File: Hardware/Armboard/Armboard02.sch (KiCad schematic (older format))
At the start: 11 parts

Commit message: Imported footprints to layout
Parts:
- Gripper_Motor1: footprint (none) -> MRDT_ICs:MultiPowerSO_30
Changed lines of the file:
@@
 F 0 "Gripper_Motor1" H 5300 5237 60  0000 C CNN
 F 1 "VNH5019A_E" H 5300 5131 60  0000 C CNN
-F 2 "" H 4700 4850 60  0001 C CNN
+F 2 "MRDT_ICs:MultiPowerSO_30" H 4700 4850 60  0001 C CNN
 F 3 "" H 4700 4850 60  0001 C CNN
 	1    4700 3550

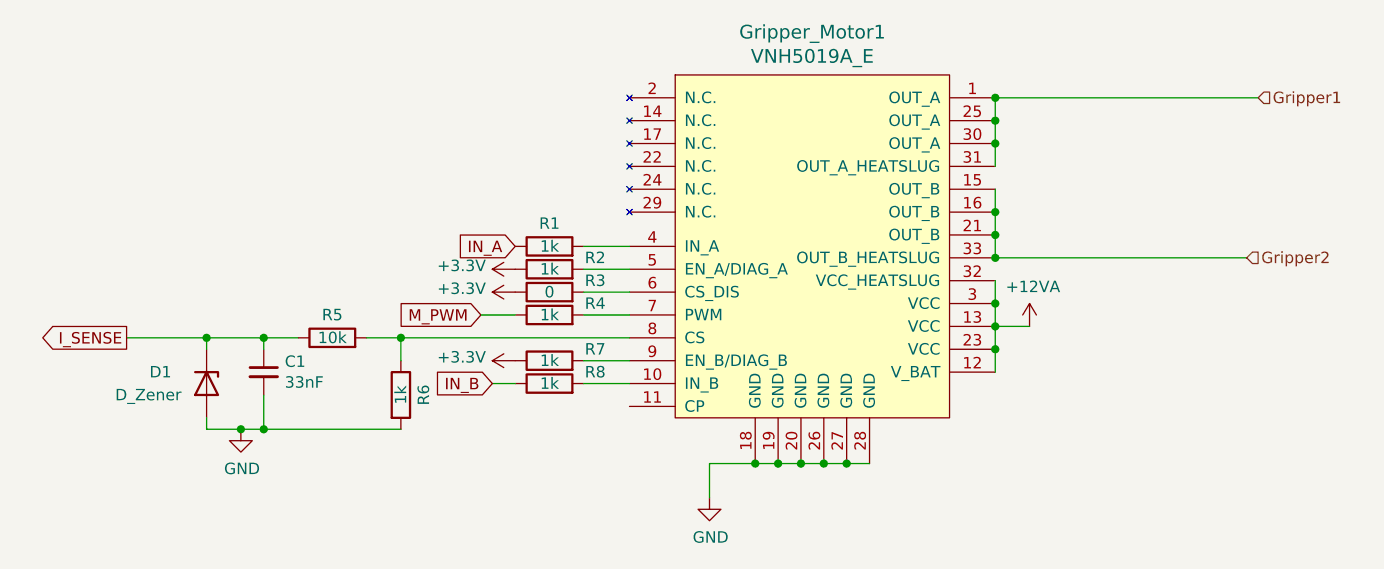
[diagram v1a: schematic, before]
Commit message: Double-checked schematic, pointed power pins up, made sure 12V and 3.3V were full networks
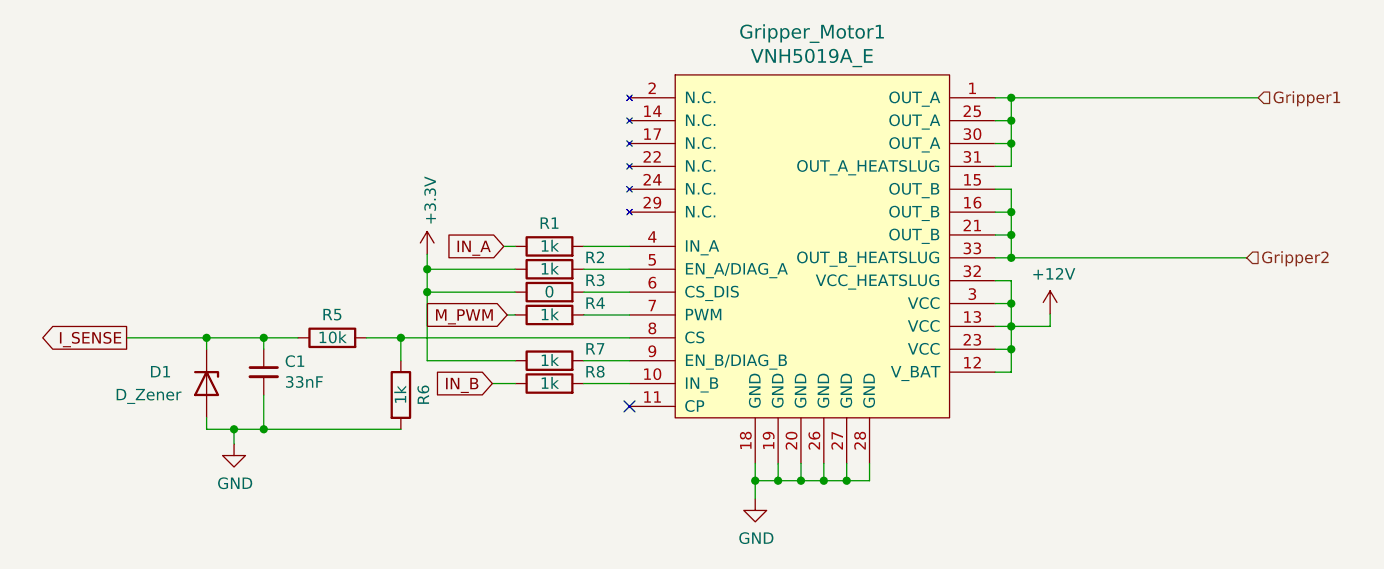
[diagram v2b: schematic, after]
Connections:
- net +12VA renamed +12V
- no-connect marks 0 -> 1
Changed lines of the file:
@@
 $EndDescr
-$Comp
-L MRDT_ICs:VNH5019A_E Gripper_Motor1
-U 1 1 5F7F9831
-P 4700 3550
-F 0 "Gripper_Motor1" H 5300 5237 60  0000 C CNN
-F 1 "VNH5019A_E" H 5300 5131 60  0000 C CNN
-F 2 "MRDT_ICs:MultiPowerSO_30" H 4700 4850 60  0001 C CNN
-F 3 "" H 4700 4850 60  0001 C CNN
-	1    4700 3550
-	1    0    0    -1
-$EndComp
 $Comp
 L power:GND #PWR074
 U 1 1 5F7FB309
-P 4850 3900
-F 0 "#PWR074" H 4850 3650 50  0001 C CNN
-F 1 "GND" H 4855 3727 50  0000 C CNN
-F 2 "" H 4850 3900 50  0001 C CNN
-F 3 "" H 4850 3900 50  0001 C CNN
-	1    4850 3900
-	1    0    0    -1
-$EndComp
-Wire Wire Line
-	5550 3750 5450 3750
-Connection ~ 5150 3750
-Wire Wire Line
-	5150 3750 5050 3750
-Connection ~ 5250 3750
-Wire Wire Line
-	5250 3750 5150 3750
-Connection ~ 5350 3750
-Wire Wire Line
-	5350 3750 5250 3750
-Connection ~ 5450 3750
-Wire Wire Line
-	5450 3750 5350 3750
-Wire Wire Line
-	5050 3750 4850 3750
-Wire Wire Line
-	4850 3750 4850 3900
-Connection ~ 5050 3750
-Wire Wire Line
-	6100 2150 6100 2250
-Connection ~ 6100 2250
-Wire Wire Line
-	6100 2250 6100 2350
-Connection ~ 6100 2350
-Wire Wire Line
-	6100 2350 6100 2450
-Connection ~ 6100 2150
-Wire Wire Line
-	6100 2550 6100 2650
-Connection ~ 6100 2650
-Wire Wire Line
-	6100 2650 6100 2750
-Connection ~ 6100 2750
-Wire Wire Line
-	6100 2750 6100 2850
-Wire Wire Line
-	6100 2950 6100 3050
-Connection ~ 6100 3050
-Wire Wire Line
-	6100 3050 6100 3150
-Connection ~ 6100 3150
-Wire Wire Line
-	6100 3150 6100 3250
-Connection ~ 6100 3250
-Wire Wire Line
-	6100 3250 6100 3350
-Wire Wire Line
-	6100 3150 6250 3150
-$Comp
-L power:+12VA #PWR075
-U 1 1 5F7FD222
-P 6250 3150
-F 0 "#PWR075" H 6250 3000 50  0001 C CNN
-F 1 "+12VA" H 6265 3323 50  0000 C CNN
-F 2 "" H 6250 3150 50  0001 C CNN
-F 3 "" H 6250 3150 50  0001 C CNN
-	1    6250 3150
+P 5050 3905
+F 0 "#PWR074" H 5050 3655 50  0001 C CNN
+F 1 "GND" H 5055 3732 50  0000 C CNN
+F 2 "" H 5050 3905 50  0001 C CNN
+F 3 "" H 5050 3905 50  0001 C CNN
+	1    5050 3905
 	1    0    0    -1
 $EndComp
@@
 L power:+3.3V #PWR071
 U 1 1 5F802765
-P 4000 2900
-F 0 "#PWR071" H 4000 2750 50  0001 C CNN
-F 1 "+3.3V" V 4015 3028 50  0000 L CNN
-F 2 "" H 4000 2900 50  0001 C CNN
-F 3 "" H 4000 2900 50  0001 C CNN
-	1    4000 2900
-	0    -1   -1   0
+P 3615 2835
+F 0 "#PWR071" H 3615 2685 50  0001 C CNN
+F 1 "+3.3V" V 3630 2963 50  0000 L CNN
+F 2 "" H 3615 2835 50  0001 C CNN
+F 3 "" H 3615 2835 50  0001 C CNN
+	1    3615 2835
+	1    0    0    -1
 $EndComp
 $Comp
@@
 	0    -1   -1   0
 $EndComp
-$Comp
-L power:+3.3V #PWR072
-U 1 1 5F807CCC
-P 4000 3000
-F 0 "#PWR072" H 4000 2850 50  0001 C CNN
-F 1 "+3.3V" V 4015 3128 50  0000 L CNN
-F 2 "" H 4000 3000 50  0001 C CNN
-F 3 "" H 4000 3000 50  0001 C CNN
-	1    4000 3000
-	0    -1   -1   0
-$EndComp
 Wire Wire Line
 	4300 3100 4500 3100
@@
 L power:GND #PWR070
 U 1 1 5F80DDCF
-P 2800 3600
-F 0 "#PWR070" H 2800 3350 50  0001 C CNN
-F 1 "GND" H 2805 3427 50  0000 C CNN
-F 2 "" H 2800 3600 50  0001 C CNN
-F 3 "" H 2800 3600 50  0001 C CNN
-	1    2800 3600
-	1    0    0    -1
-$EndComp
-Wire Wire Line
-	2900 3600 2800 3600
+P 2770 3665
+F 0 "#PWR070" H 2770 3415 50  0001 C CNN
+F 1 "GND" H 2775 3492 50  0000 C CNN
+F 2 "" H 2770 3665 50  0001 C CNN
+F 3 "" H 2770 3665 50  0001 C CNN
+	1    2770 3665
+	1    0    0    -1
+$EndComp
 Connection ~ 2900 3600
 Wire Wire Line
-	2800 3600 2650 3600
-Wire Wire Line
 	2650 3600 2650 3550
-Connection ~ 2800 3600
 Text GLabel 2300 3200 0    50   Output ~ 0
 I_SENSE
@@
 	0    -1   -1   0
 $EndComp
-$Comp
-L power:+3.3V #PWR073
-U 1 1 5F818EFA
-P 4000 3300
-F 0 "#PWR073" H 4000 3150 50  0001 C CNN
-F 1 "+3.3V" V 4015 3428 50  0000 L CNN
-F 2 "" H 4000 3300 50  0001 C CNN
-F 3 "" H 4000 3300 50  0001 C CNN
-	1    4000 3300
-	0    -1   -1   0
-$EndComp
 Wire Wire Line
 	3500 3200 4500 3200
 Wire Wire Line
-	6100 2150 7250 2150
-Connection ~ 6100 2850
-Wire Wire Line
-	6100 2850 7200 2850
-Wire Wire Line
-	3850 3100 4000 3100
+	6100 2150 6170 2150
+Wire Wire Line
+	6100 2850 6170 2850
 Wire Wire Line
 	4000 3400 3900 3400
 Text GLabel 3900 3400 0    50   Input ~ 0
 IN_B
-Text GLabel 4000 2800 0    50   Input ~ 0
+Text GLabel 3950 2800 0    50   Input ~ 0
 IN_A
-Text GLabel 3850 3100 0    50   Input ~ 0
+Text GLabel 3965 3100 0    50   Input ~ 0
 M_PWM
 Text HLabel 7250 2150 2    50   Input ~ 0
@@
 	0    1    1    0
 $EndComp
+Wire Wire Line
+	4000 3000 3615 3000
+Wire Wire Line
+	3615 3000 3615 2900
+Wire Wire Line
+	4000 2900 3615 2900
+Connection ~ 3615 2900
+Wire Wire Line
+	3615 2900 3615 2835
+Wire Wire Line
+	4000 3100 3965 3100
+Wire Wire Line
+	3615 3300 3615 3000
+Connection ~ 3615 3000
+NoConn ~ 4500 3500
+Wire Wire Line
+	6100 2450 6170 2450
+Connection ~ 6170 2150
+Wire Wire Line
+	6170 2150 7250 2150
+Wire Wire Line
+	6100 2250 6170 2250
+Wire Wire Line
+	6170 2150 6170 2250
+Connection ~ 6170 2250
+Wire Wire Line
+	6170 2250 6170 2350
+Wire Wire Line
+	6100 2350 6170 2350
+Connection ~ 6170 2350
+Wire Wire Line
+	6170 2350 6170 2450
+Wire Wire Line
+	6100 2550 6170 2550
+Wire Wire Line
+	6170 2550 6170 2650
+Connection ~ 6170 2850
+Wire Wire Line
+	6170 2850 7200 2850
+$Comp
+L MRDT_ICs:VNH5019A_E Gripper_Motor1
+U 1 1 5F7F9831
+P 4700 3550
+F 0 "Gripper_Motor1" H 5300 5237 60  0000 C CNN
+F 1 "VNH5019A_E" H 5300 5131 60  0000 C CNN
+F 2 "MRDT_ICs:MultiPowerSO_30" H 4700 4850 60  0001 C CNN
+F 3 "" H 4700 4850 60  0001 C CNN
+	1    4700 3550
+	1    0    0    -1
+$EndComp
+Wire Wire Line
+	6100 2650 6170 2650
+Connection ~ 6170 2650
+Wire Wire Line
+	6100 2750 6170 2750
+Wire Wire Line
+	6170 2650 6170 2750
+Connection ~ 6170 2750
+Wire Wire Line
+	6170 2750 6170 2850
+Wire Wire Line
+	6100 2950 6170 2950
+Wire Wire Line
+	6170 2950 6170 3050
+Wire Wire Line
+	6170 3350 6100 3350
+Wire Wire Line
+	6170 3150 6340 3150
+Connection ~ 6170 3150
+Wire Wire Line
+	6170 3150 6170 3250
+Wire Wire Line
+	6100 3050 6170 3050
+Connection ~ 6170 3050
+Wire Wire Line
+	6170 3050 6170 3150
+Wire Wire Line
+	6100 3250 6170 3250
+Connection ~ 6170 3250
+Wire Wire Line
+	6170 3250 6170 3350
+Wire Wire Line
+	6100 3150 6170 3150
+Wire Wire Line
+	3950 2800 4000 2800
+Wire Wire Line
+	2770 3665 2770 3600
+Wire Wire Line
+	2650 3600 2770 3600
+Connection ~ 2770 3600
+Wire Wire Line
+	2770 3600 2900 3600
+Wire Wire Line
+	5050 3905 5050 3825
+Wire Wire Line
+	5050 3825 5150 3825
+Wire Wire Line
+	5550 3825 5550 3750
+Connection ~ 5050 3825
+Wire Wire Line
+	5050 3825 5050 3750
+Wire Wire Line
+	5150 3750 5150 3825
+Connection ~ 5150 3825
+Wire Wire Line
+	5150 3825 5250 3825
+Wire Wire Line
+	5250 3750 5250 3825
+Connection ~ 5250 3825
+Wire Wire Line
+	5250 3825 5350 3825
+Wire Wire Line
+	5350 3750 5350 3825
+Connection ~ 5350 3825
+Wire Wire Line
+	5350 3825 5450 3825
+Wire Wire Line
+	5450 3750 5450 3825
+Connection ~ 5450 3825
+Wire Wire Line
+	5450 3825 5550 3825
+$Comp
+L power:+12V #PWR0102
+U 1 1 5FBD4460
+P 6340 3095
+F 0 "#PWR0102" H 6340 2945 50  0001 C CNN
+F 1 "+12V" H 6355 3268 50  0000 C CNN
+F 2 "" H 6340 3095 50  0001 C CNN
+F 3 "" H 6340 3095 50  0001 C CNN
+	1    6340 3095
+	1    0    0    -1
+$EndComp
+Wire Wire Line
+	6340 3150 6340 3095
+Wire Wire Line
+	3615 3300 4000 3300
 $EndSCHEMATC

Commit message: Fixed some library issues and moved Gerbs to Manufacturing folder
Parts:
- C1: footprint Capacitor_SMD:C_0603_1608Metric_Pad1.05x0.95mm_HandSolder -> Capacitor_SMD:C_0603_1608Metric_Pad1.08x0.95mm_HandSolder
- R1, R2, R3, R4, R5, R6, R7, R8: footprint Resistor_SMD:R_0603_1608Metric_Pad1.05x0.95mm_HandSolder -> Resistor_SMD:R_0603_1608Metric_Pad0.98x0.95mm_HandSolder
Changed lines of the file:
@@
 EESchema Schematic File Version 4
+LIBS:Armboard-cache
 EELAYER 30 0
 EELAYER END
@@
 F 0 "R1" V 4250 2800 50  0000 C CNN
 F 1 "1k" V 4150 2800 50  0000 C CNN
-F 2 "Resistor_SMD:R_0603_1608Metric_Pad1.05x0.95mm_HandSolder" V 4080 2800 50  0001 C CNN
+F 2 "Resistor_SMD:R_0603_1608Metric_Pad0.98x0.95mm_HandSolder" V 4080 2800 50  0001 C CNN
 F 3 "~" H 4150 2800 50  0001 C CNN
 	1    4150 2800
@@
 F 0 "R2" V 4200 2700 50  0000 C CNN
 F 1 "1k" V 4150 2900 50  0000 C CNN
-F 2 "Resistor_SMD:R_0603_1608Metric_Pad1.05x0.95mm_HandSolder" V 4080 2900 50  0001 C CNN
+F 2 "Resistor_SMD:R_0603_1608Metric_Pad0.98x0.95mm_HandSolder" V 4080 2900 50  0001 C CNN
 F 3 "~" H 4150 2900 50  0001 C CNN
 	1    4150 2900
@@
 F 0 "R3" V 4200 2800 50  0000 C CNN
 F 1 "0" V 4150 3000 50  0000 C CNN
-F 2 "Resistor_SMD:R_0603_1608Metric_Pad1.05x0.95mm_HandSolder" V 4080 3000 50  0001 C CNN
+F 2 "Resistor_SMD:R_0603_1608Metric_Pad0.98x0.95mm_HandSolder" V 4080 3000 50  0001 C CNN
 F 3 "~" H 4150 3000 50  0001 C CNN
 	1    4150 3000
@@
 F 0 "R4" V 4200 2900 50  0000 C CNN
 F 1 "1k" V 4150 3100 50  0000 C CNN
-F 2 "Resistor_SMD:R_0603_1608Metric_Pad1.05x0.95mm_HandSolder" V 4080 3100 50  0001 C CNN
+F 2 "Resistor_SMD:R_0603_1608Metric_Pad0.98x0.95mm_HandSolder" V 4080 3100 50  0001 C CNN
 F 3 "~" H 4150 3100 50  0001 C CNN
 	1    4150 3100
@@
 F 0 "R5" V 3300 3200 50  0000 C CNN
 F 1 "10k" V 3200 3200 50  0000 C CNN
-F 2 "Resistor_SMD:R_0603_1608Metric_Pad1.05x0.95mm_HandSolder" V 3130 3200 50  0001 C CNN
+F 2 "Resistor_SMD:R_0603_1608Metric_Pad0.98x0.95mm_HandSolder" V 3130 3200 50  0001 C CNN
 F 3 "~" H 3200 3200 50  0001 C CNN
 	1    3200 3200
@@
 F 0 "R6" V 3600 3450 50  0000 C CNN
 F 1 "1k" V 3500 3450 50  0000 C CNN
-F 2 "Resistor_SMD:R_0603_1608Metric_Pad1.05x0.95mm_HandSolder" V 3430 3450 50  0001 C CNN
+F 2 "Resistor_SMD:R_0603_1608Metric_Pad0.98x0.95mm_HandSolder" V 3430 3450 50  0001 C CNN
 F 3 "~" H 3500 3450 50  0001 C CNN
 	1    3500 3450
@@
 F 0 "C1" H 2992 3396 50  0000 L CNN
 F 1 "33nF" H 2992 3305 50  0000 L CNN
-F 2 "Capacitor_SMD:C_0603_1608Metric_Pad1.05x0.95mm_HandSolder" H 2900 3350 50  0001 C CNN
+F 2 "Capacitor_SMD:C_0603_1608Metric_Pad1.08x0.95mm_HandSolder" H 2900 3350 50  0001 C CNN
 F 3 "~" H 2900 3350 50  0001 C CNN
 	1    2900 3350
@@
 F 0 "R7" V 4200 3100 50  0000 C CNN
 F 1 "1k" V 4150 3300 50  0000 C CNN
-F 2 "Resistor_SMD:R_0603_1608Metric_Pad1.05x0.95mm_HandSolder" V 4080 3300 50  0001 C CNN
+F 2 "Resistor_SMD:R_0603_1608Metric_Pad0.98x0.95mm_HandSolder" V 4080 3300 50  0001 C CNN
 F 3 "~" H 4150 3300 50  0001 C CNN
 	1    4150 3300
@@
 F 0 "R8" V 4200 3200 50  0000 C CNN
 F 1 "1k" V 4150 3400 50  0000 C CNN
-F 2 "Resistor_SMD:R_0603_1608Metric_Pad1.05x0.95mm_HandSolder" V 4080 3400 50  0001 C CNN
+F 2 "Resistor_SMD:R_0603_1608Metric_Pad0.98x0.95mm_HandSolder" V 4080 3400 50  0001 C CNN
 F 3 "~" H 4150 3400 50  0001 C CNN
 	1    4150 3400
